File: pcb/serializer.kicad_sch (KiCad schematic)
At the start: 26 parts, among them U3 DS90UB9x3

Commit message: Inital routing complete
- Addressed Aaron's review
- Pullup on output side of analog switch to prevent floating SDA
- Other minor changes
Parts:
- renumbered C11 to C10, C12 to C11, C13 to C12, C14 to C13, C15 to C14, C16 to C15, C17 to C16, C18 to C17, C19 to C18, C20 to C19, C21 to C20, C22 to C21, C7 to C6, C8 to C7, C9 to C8, C10 to C9, R5 to R3, R6 to R4, R8 to R5, R7 to R6, R10 to R7
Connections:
- net Dout-: now reaches C20.2, R7.1
- net DOut renamed DOut+
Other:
- moved on the sheet: C21, D1, R3, R5, R6

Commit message: Address team comments
- Add extra mouse-bite supports
- Enbiggen cable strain relief spear
- Add DNP 0.1" header for bench debug
- Small routing changes
- Update and complete BOM
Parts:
- C10, C13, C16, C19, C20, C21, C6, C8, L3, L4: CASE/PACKAGE (none) -> 0201
- C11, C14, C17, C7, C9: CASE/PACKAGE (none) -> 0201; Voltage 16V -> 25V
- C12, C15, C18: CASE/PACKAGE (none) -> 0402
- JP1: now left out of the parts list
- R3, R4, R5, R6, R7: CASE/PACKAGE (none) -> 0201; Tolerance (none) -> 1%
- U3: CASE/PACKAGE WQFN -> (none)

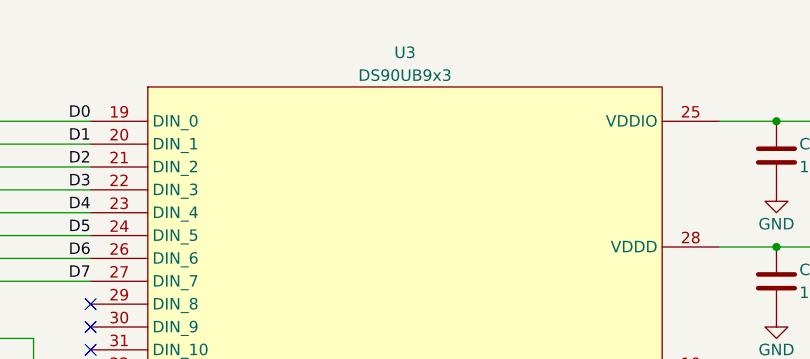
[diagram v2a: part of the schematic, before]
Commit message: Updates to design after feedback from assembler
- Replace obsolete TE_2013496-9 ZIF connector used by IMEC with
046844727002846+, which should fit NP 2.0 flex connectors (see design
folder for comparison). We will see.
- Replaced programmable MEMS oscillator with standard quartz since this
is a common frequency.
- Other BOM updates to account for obsolete or out of stock components
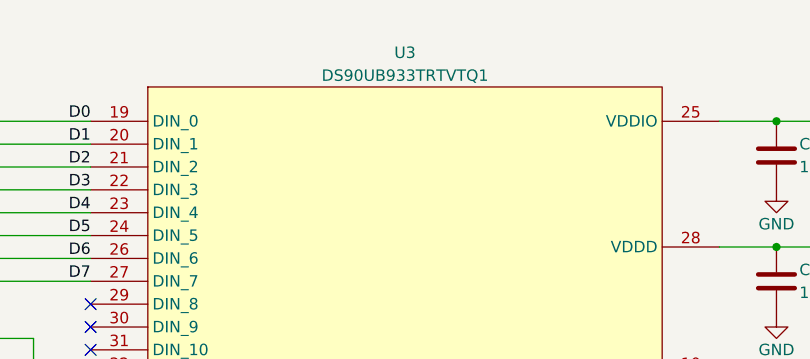
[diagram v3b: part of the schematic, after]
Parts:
- U3: value DS90UB9x3 -> DS90UB933TRTVTQ1
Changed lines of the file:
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@@
       (effects (font (size 1.27 1.27)))
     )
-    (property "Value" "DS90UB9x3" (at 155.575 43.18 0)
+    (property "Value" "DS90UB933TRTVTQ1" (at 155.575 43.18 0)
       (effects (font (size 1.27 1.27)))
     )
